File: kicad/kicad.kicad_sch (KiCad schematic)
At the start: 28 parts, among them J101 DEBUG_LED_CONN, J102 EPD_SPI_CONN, J103 HPC_CONN, J104 STORAGE_CONN, J105 MGMT_CONN, J106 GLOBAL_CONN, J107 INPUT_CONN, J109 USBC_CONN

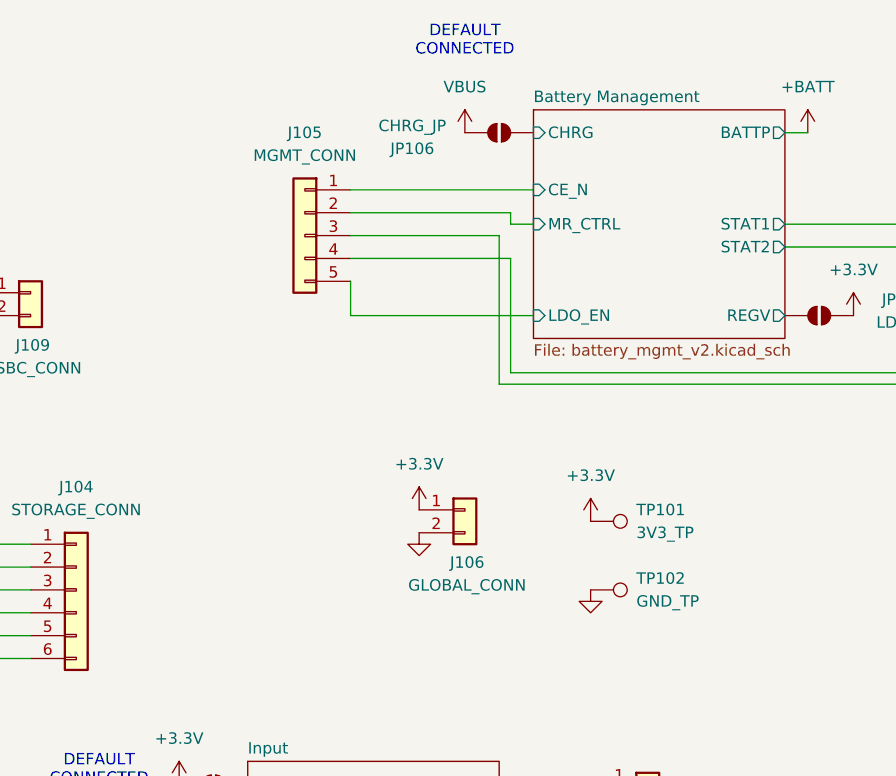
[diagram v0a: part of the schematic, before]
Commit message: finish management schematic, ready for PCB
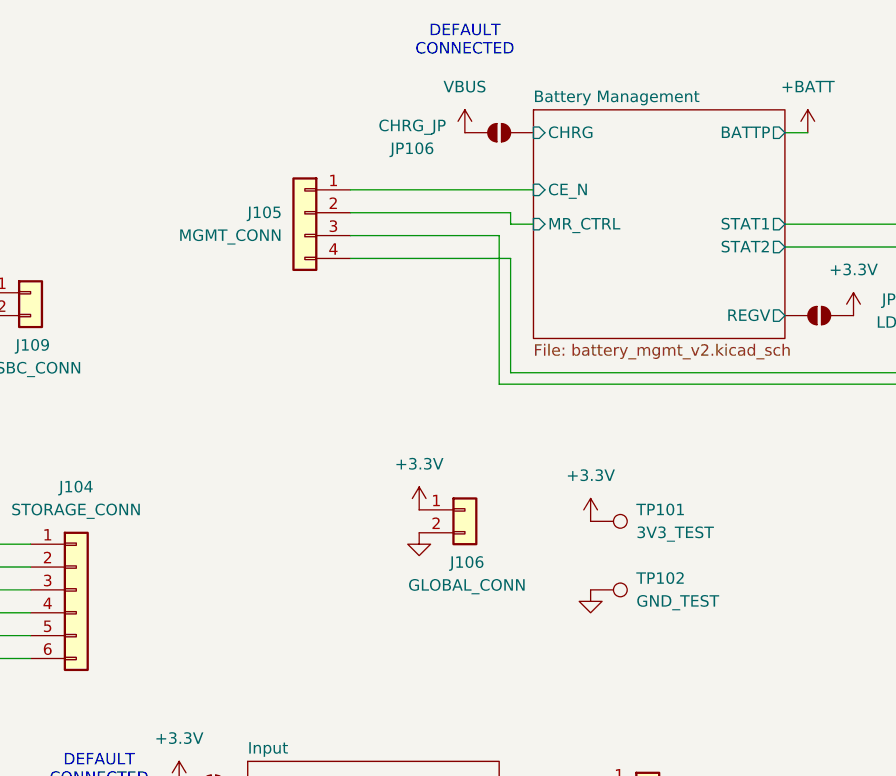
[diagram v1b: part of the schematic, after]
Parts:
- removed J105: MGMT_CONN, symbol Connector_Generic:Conn_01x05
- added J105: MGMT_CONN, Connector_JST:JST_XH_B4B-XH-A_1x04_P2.50mm_Vertical, symbol Connector_Generic:Conn_01x04
- TP101: value 3V3_TP -> 3V3_TEST
- TP102: value GND_TP -> GND_TEST
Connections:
- net Battery Management/CE_N: now also J105.1 (Pin_1)
- net Battery Management/MR_CTRL: now also J105.2 (Pin_2)
- net Battery Management/STAT1: now also J105.3 (Pin_3)
- net Battery Management/STAT2: now also J105.4 (Pin_4)
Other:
- sheet Battery Management ports: added none; removed LDO_EN
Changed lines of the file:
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@@
 	(wire
 		(pts
-			(xy 194.31 62.23) (xy 194.31 66.04)
-		)
-		(stroke
-			(width 0)
-			(type default)
-		)
-	)
-	(wire
-		(pts
 			(xy 83.82 45.72) (xy 81.28 45.72)
 		)
@@
 	(wire
 		(pts
-			(xy 194.31 66.04) (xy 214.63 66.04)
-		)
-		(stroke
-			(width 0)
-			(type default)
-		)
-	)
-	(wire
-		(pts
 			(xy 210.82 73.66) (xy 261.62 73.66)
 		)
@@
 	)
 	(symbol
-		(lib_id "Connector_Generic:Conn_01x05")
-		(at 189.23 57.15 0)
-		(mirror y)
-		(unit 1)
-		(exclude_from_sim no)
-		(in_bom yes)
-		(on_board yes)
-		(dnp no)
-		(fields_autoplaced yes)
-		(property "Reference" "J105"
-			(at 189.23 45.72 0)
-			(effects
-				(font
-					(size 1.27 1.27)
-				)
-			)
-		)
-		(property "Value" "MGMT_CONN"
-			(at 189.23 48.26 0)
-			(effects
-				(font
-					(size 1.27 1.27)
-				)
-			)
-		)
-		(property "Footprint" ""
-			(at 189.23 57.15 0)
-			(effects
-				(font
-					(size 1.27 1.27)
-				)
-				(hide yes)
-			)
-		)
-		(property "Datasheet" "~"
-			(at 189.23 57.15 0)
-			(effects
-				(font
-					(size 1.27 1.27)
-				)
-				(hide yes)
-			)
-		)
-		(property "Description" "Generic connector, single row, 01x05, script generated (kicad-library-utils/schlib/autogen/connector/)"
-			(at 189.23 57.15 0)
-			(effects
-				(font
-					(size 1.27 1.27)
-				)
-				(hide yes)
-			)
-		)
-		(pin "5"
-		)
-		(pin "3"
-		)
-		(pin "1"
-		)
-		(pin "2"
-		)
-		(pin "4"
-		)
-		(instances
-			(project "kicad"
-				(path "/97e37379-fec6-4f0d-82d9-4ea53516bb02"
-					(reference "J105")
-					(unit 1)
-				)
-			)
-		)
-	)
-	(symbol
 		(lib_id "Device:R")
 		(at 63.5 104.14 0)
@@
 	)
 	(symbol
+		(lib_id "Connector_Generic:Conn_01x04")
+		(at 189.23 54.61 0)
+		(mirror y)
+		(unit 1)
+		(exclude_from_sim no)
+		(in_bom yes)
+		(on_board yes)
+		(dnp no)
+		(property "Reference" "J105"
+			(at 186.69 54.6099 0)
+			(effects
+				(font
+					(size 1.27 1.27)
+				)
+				(justify left)
+			)
+		)
+		(property "Value" "MGMT_CONN"
+			(at 186.69 57.1499 0)
+			(effects
+				(font
+					(size 1.27 1.27)
+				)
+				(justify left)
+			)
+		)
+		(property "Footprint" "Connector_JST:JST_XH_B4B-XH-A_1x04_P2.50mm_Vertical"
+			(at 189.23 54.61 0)
+			(effects
+				(font
+					(size 1.27 1.27)
+				)
+				(hide yes)
+			)
+		)
+		(property "Datasheet" "~"
+			(at 189.23 54.61 0)
+			(effects
+				(font
+					(size 1.27 1.27)
+				)
+				(hide yes)
+			)
+		)
+		(property "Description" "Generic connector, single row, 01x04, script generated (kicad-library-utils/schlib/autogen/connector/)"
+			(at 189.23 54.61 0)
+			(effects
+				(font
+					(size 1.27 1.27)
+				)
+				(hide yes)
+			)
+		)
+		(property "JLC" "XXXXXX"
+			(at 189.23 54.61 0)
+			(effects
+				(font
+					(size 1.27 1.27)
+				)
+				(hide yes)
+			)
+		)
+		(property "LCSC" "XXXXXX"
+			(at 189.23 54.61 0)
+			(effects
+				(font
+					(size 1.27 1.27)
+				)
+				(hide yes)
+			)
+		)
+		(pin "2"
+		)
+		(pin "4"
+		)
+		(pin "3"
+		)
+		(pin "1"
+		)
+		(instances
+			(project "kicad"
+				(path "/97e37379-fec6-4f0d-82d9-4ea53516bb02"
+					(reference "J105")
+					(unit 1)
+				)
+			)
+		)
+	)
+	(symbol
 		(lib_id "Connector_Generic:Conn_01x02")
 		(at 158.75 63.5 0)
@@
 			)
 		)
-		(property "Value" "GND_TP"
+		(property "Value" "GND_TEST"
 			(at 226.06 97.7899 90)
 			(effects
@@
 			)
 		)
-		(property "Value" "3V3_TP"
+		(property "Value" "3V3_TEST"
 			(at 226.06 90.1699 90)
 			(effects
@@
 			(effects
 				(font
-					(size 1.27 1.27)
-				)
-				(justify left)
-			)
-		)
-		(pin "LDO_EN" input
-			(at 214.63 66.04 180)
-			(effects
-				(font

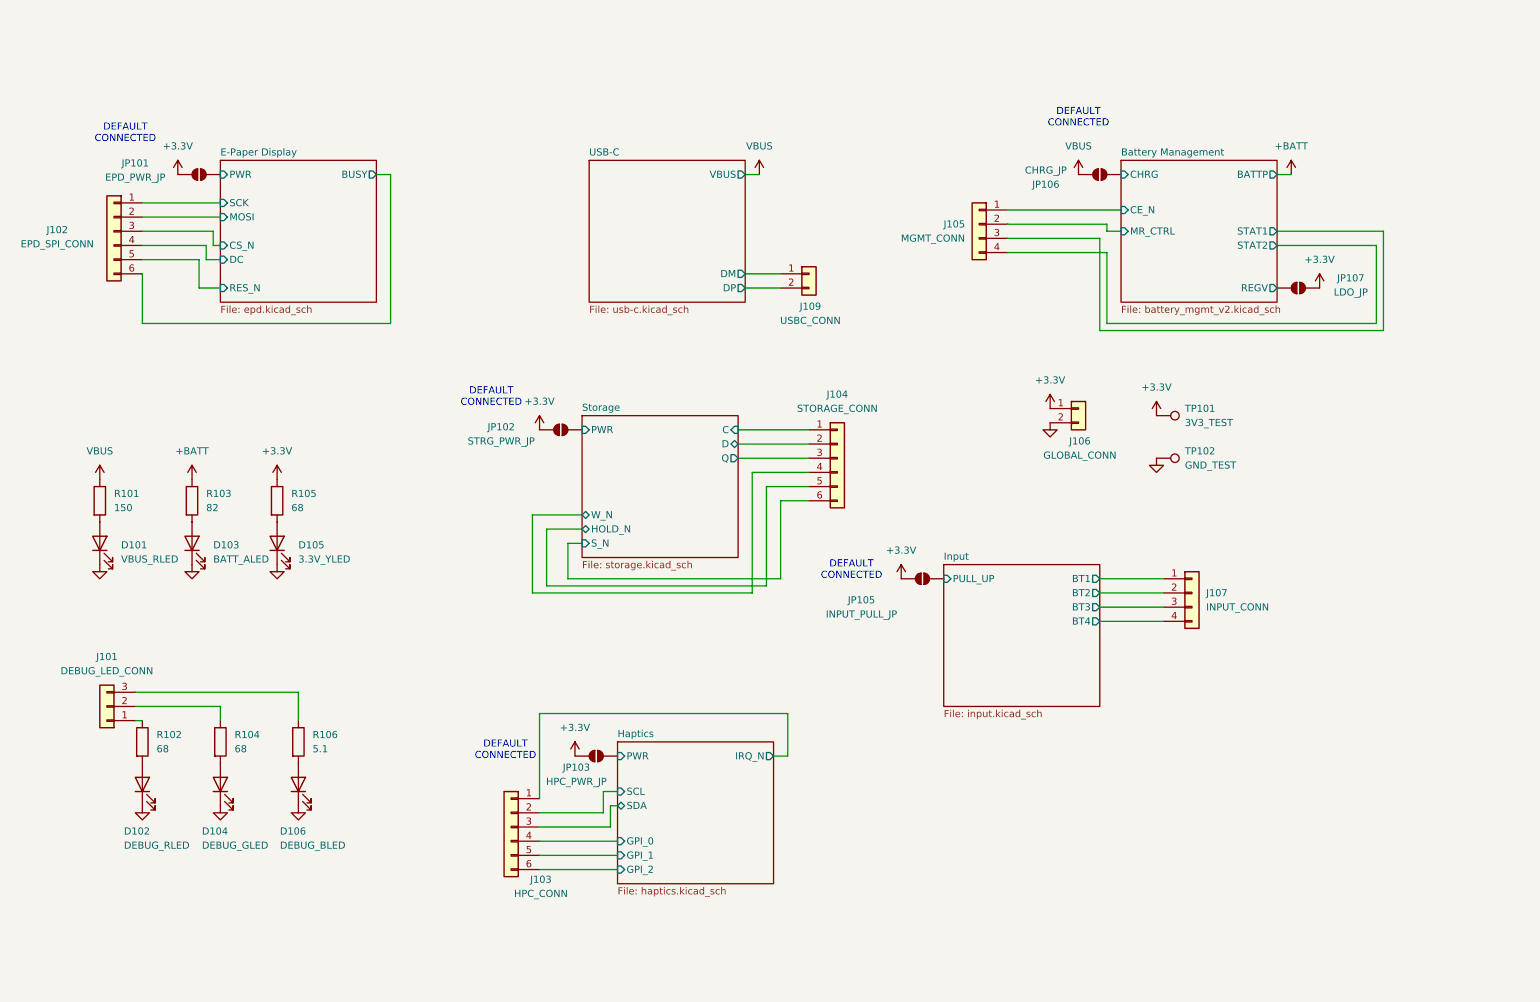
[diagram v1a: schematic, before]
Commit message: finish battery PCB layout, PCB refactoring
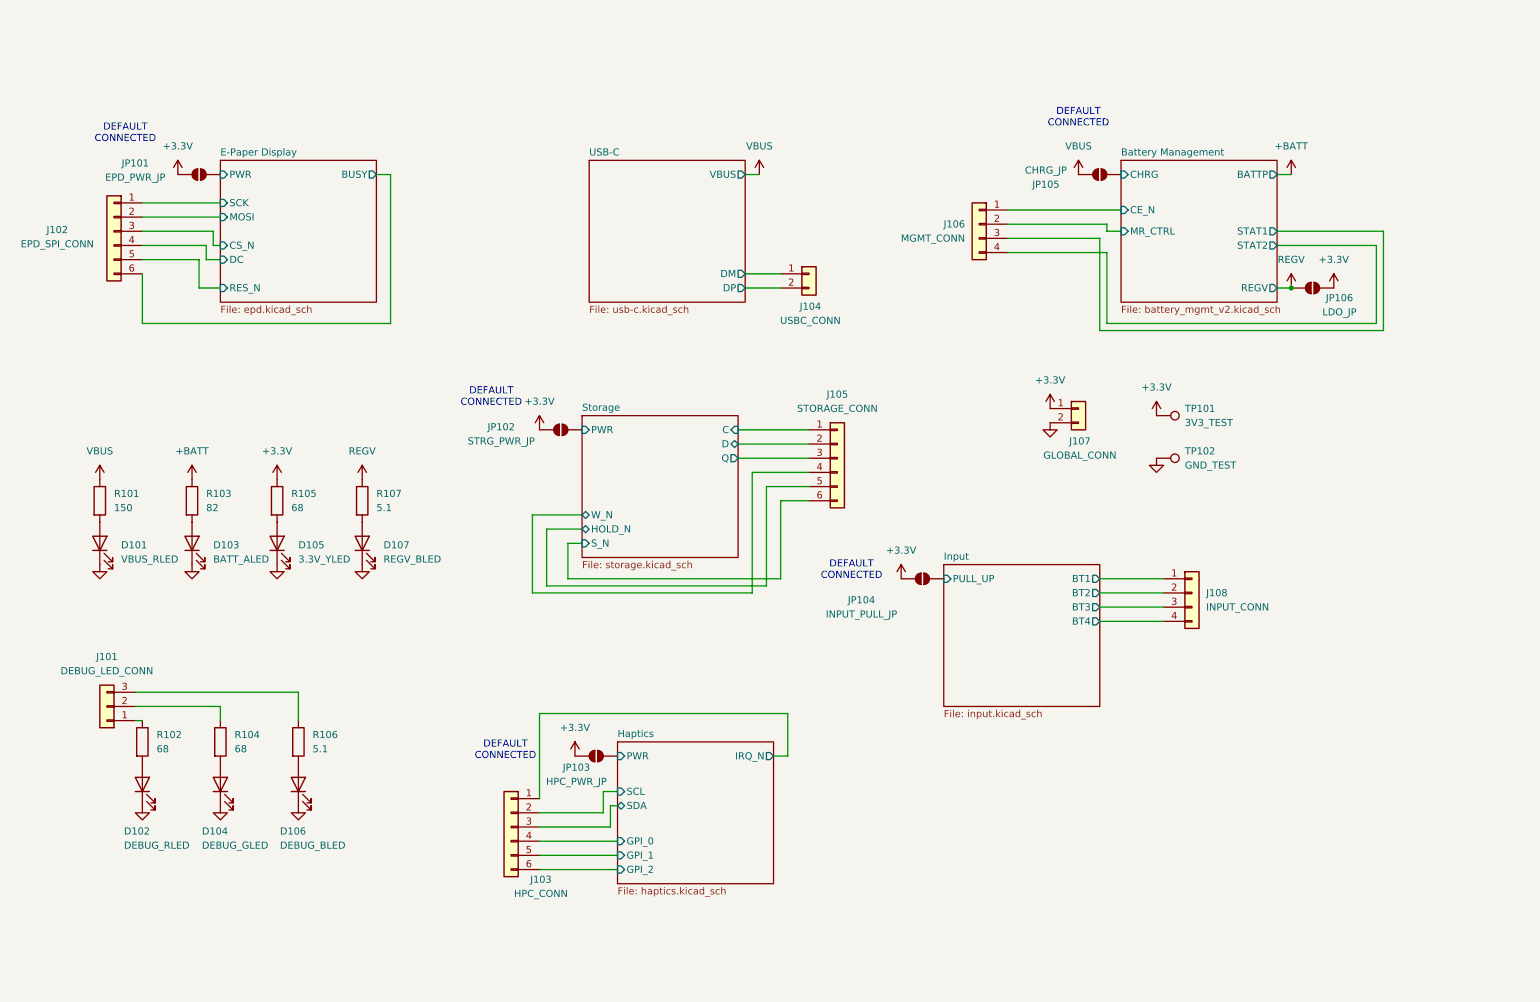
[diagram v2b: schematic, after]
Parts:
- added D107: REGV_BLED, Diode_SMD:D_0603_1608Metric_Pad1.05x0.95mm_HandSolder, symbol Device:LED
- added R107: 5.1, Resistor_SMD:R_0603_1608Metric_Pad0.98x0.95mm_HandSolder, symbol Device:R
- renumbered J109 to J104, J104 to J105, J105 to J106, J106 to J107, J107 to J108, JP105 to JP104, JP106 to JP105, JP107 to JP106
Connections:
- net GND: now also D107.1 (K)
- net Battery Management/REGV renamed REGV
- net REGV: now also R107.1
- new net: D107.2 (A), R107.2
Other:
- moved on the sheet: JP106

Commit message: Revision 2: Fix MOSFET pins and various changes
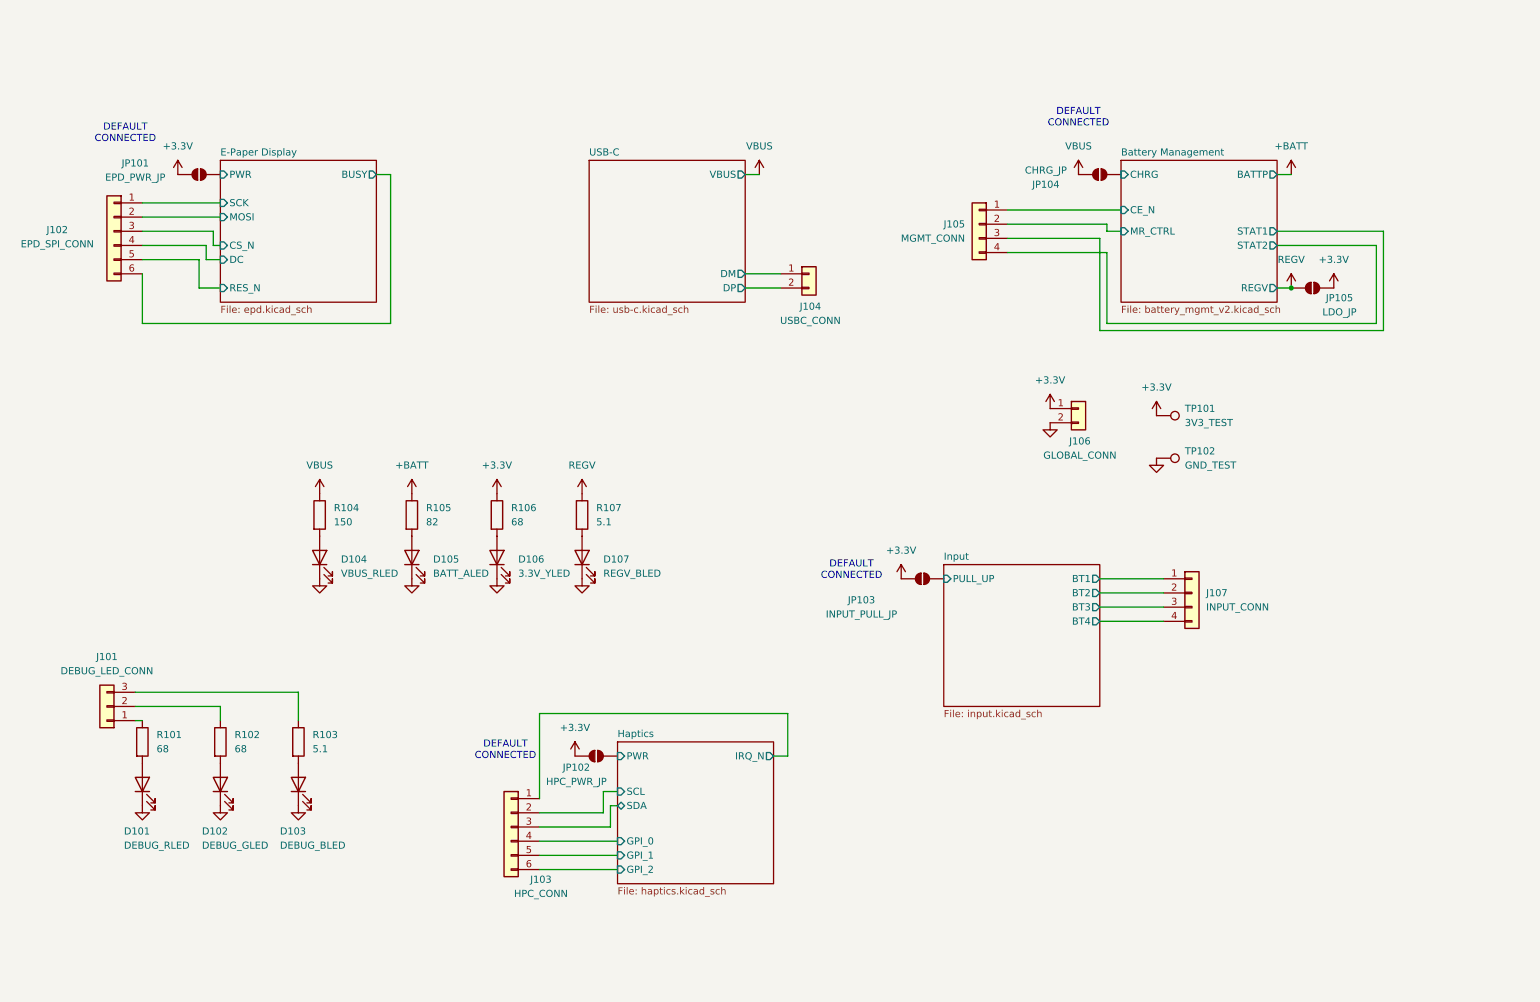
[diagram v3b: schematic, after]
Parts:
- removed J105: STORAGE_CONN, Connector_JST:JST_XH_B6B-XH-A_1x06_P2.50mm_Vertical, symbol Connector_Generic:Conn_01x06
- removed JP102: STRG_PWR_JP, Jumper:SolderJumper-2_P1.3mm_Open_TrianglePad1.0x1.5mm, symbol Jumper:SolderJumper_2_Open
- renumbered D102 to D101, D104 to D102, D106 to D103, D101 to D104, D103 to D105, D105 to D106, J106 to J105, J107 to J106, J108 to J107, JP103 to JP102, JP104 to JP103, JP105 to JP104, JP106 to JP105, R102 to R101, R104 to R102, R106 to R103, R101 to R104, R103 to R105, R105 to R106
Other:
- removed sheet Storage
- moved on the sheet: D104, D105, D106, D107, R104, R105, R106, R107

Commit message: Rev. 3: Fix issues
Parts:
- removed D104: VBUS_RLED, Diode_SMD:D_0603_1608Metric_Pad1.05x0.95mm_HandSolder, symbol Device:LED
- removed D105: BATT_ALED, Diode_SMD:D_0603_1608Metric_Pad1.05x0.95mm_HandSolder, symbol Device:LED
- removed D106: 3.3V_YLED, Diode_SMD:D_0603_1608Metric_Pad1.05x0.95mm_HandSolder, symbol Device:LED
- removed D107: REGV_BLED, Diode_SMD:D_0603_1608Metric_Pad1.05x0.95mm_HandSolder, symbol Device:LED
- removed R104: 150, Resistor_SMD:R_0603_1608Metric_Pad0.98x0.95mm_HandSolder, symbol Device:R
- removed R105: 82, Resistor_SMD:R_0603_1608Metric_Pad0.98x0.95mm_HandSolder, symbol Device:R
- removed R106: 68, Resistor_SMD:R_0603_1608Metric_Pad0.98x0.95mm_HandSolder, symbol Device:R
- removed R107: 5.1, Resistor_SMD:R_0603_1608Metric_Pad0.98x0.95mm_HandSolder, symbol Device:R
- D101: value DEBUG_RLED -> NOTIFY_RLED
- D102: value DEBUG_GLED -> NOTIFY_GLED
- D103: value DEBUG_BLED -> NOTIFY_BLED
- J101: value DEBUG_LED_CONN -> NOTIFY_LED_CONN
- R101, R102: value 68 -> 560
- R103: value 5.1 -> 560
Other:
- moved on the sheet: J103, JP102

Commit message: start microcontroller schematic
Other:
- added sheet Microcontroller (microcontroller.kicad_sch)
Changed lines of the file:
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@@
+	)
+	(sheet
+		(at 250.19 87.63)
+		(size 29.21 45.72)
+		(fields_autoplaced yes)
+		(stroke
+			(width 0.1524)
+			(type solid)
+		)
+		(fill
+			(color 0 0 0 0.0000)
+		)
+		(property "Sheetname" "Microcontroller"
+			(at 250.19 86.9184 0)
+			(effects
+				(font
+					(size 1.27 1.27)
+				)
+				(justify left bottom)
+			)
+		)
+		(property "Sheetfile" "microcontroller.kicad_sch"
+			(at 250.19 133.9346 0)
+			(effects
+				(font
+					(size 1.27 1.27)
+				)
+				(justify left top)
+			)
+		)
+		(instances
+			(project "kicad"
+				(path "/97e37379-fec6-4f0d-82d9-4ea53516bb02"
+					(page "7")
+				)
+			)
+		)
 	)
 	(sheet
